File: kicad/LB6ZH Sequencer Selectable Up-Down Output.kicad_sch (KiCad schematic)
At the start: 12 parts, among them J1 RCA, J10 Conn_01x03, J43 Conn_01x02, J5 1x3, SW1 SW_DPDT_x2

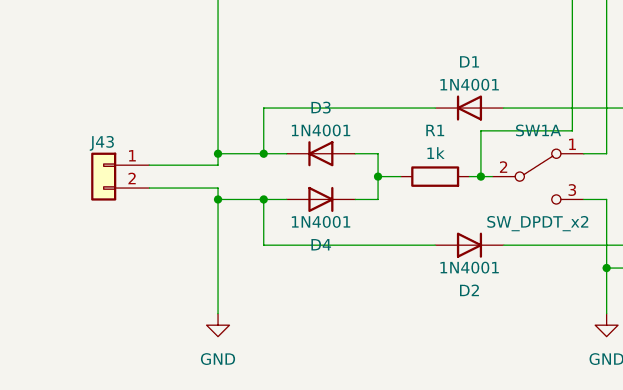
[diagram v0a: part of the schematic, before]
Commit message: Fixed a net that was grounded in error.
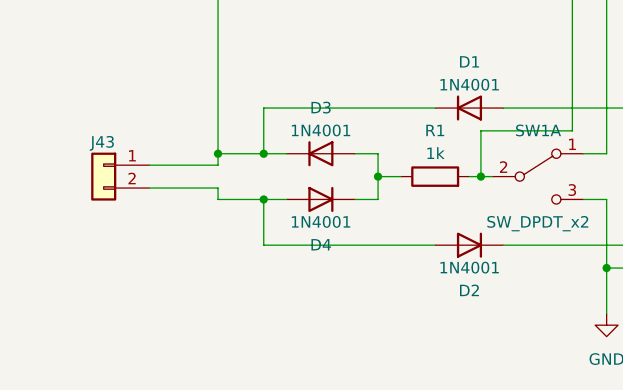
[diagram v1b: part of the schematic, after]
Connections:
- net GND: no longer D2.2 (A), D4.2 (A), J43.2 (Pin_2)
- new net: D2.2 (A), D4.2 (A), J43.2 (Pin_2)
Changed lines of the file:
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@@
   (junction (at 234.95 120.65) (diameter 0) (color 0 0 0 0)
   )
-  (junction (at 160.02 139.7) (diameter 0) (color 0 0 0 0)
-  )
   (wire (pts (xy 260.35 123.19) (xy 260.35 135.89))
     (stroke (width 0) (type default))
@@
   )
   (wire (pts (xy 203.2 110.49) (xy 203.2 134.62))
-    (stroke (width 0) (type default))
-  )
-  (wire (pts (xy 160.02 139.7) (xy 160.02 152.4))
     (stroke (width 0) (type default))
   )
@@
         )
       )
-    )
-  )
-  (symbol (lib_id "power:GND") (at 160.02 152.4 0) (unit 1)
-    (in_bom yes) (on_board yes) (dnp no) (fields_autoplaced)
-    (property "Reference" "#PWR02" (at 160.02 158.75 0)
-      (effects (font (size 1.27 1.27)) hide)
-    )
-    (property "Value" "GND" (at 160.02 157.48 0)
-      (effects (font (size 1.27 1.27)))
-    )
-    (property "Footprint" "" (at 160.02 152.4 0)
-      (effects (font (size 1.27 1.27)) hide)
-    )
-    (property "Datasheet" "" (at 160.02 152.4 0)
-      (effects (font (size 1.27 1.27)) hide)
-    )
-    (pin "1")
-    (instances
-      (project "LB6ZH Sequencer"
-        (path "/65e57460-accf-48f0-9de5-f335bec9a5fa"
-          (reference "#PWR02") (unit 1)
-        )
-        (path "/65e57460-accf-48f0-9de5-f335bec9a5fa/8125e57b-7d47-428e-81b3-59f2dce9c49e"
-          (reference "#PWR011") (unit 1)
-        )
-      )
